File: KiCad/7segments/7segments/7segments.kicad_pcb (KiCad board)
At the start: 2 copper layers, 63.5 x 59.7 mm, 19 parts, among them J1 Conn_01x04_Female, J2 12V DC, J3 R pinnen RGB strips, SW1 ENABLE, SW2 BOOT, T1 BC848, T2 BC848, T3 BC848, T4 BC848, T5 BC848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

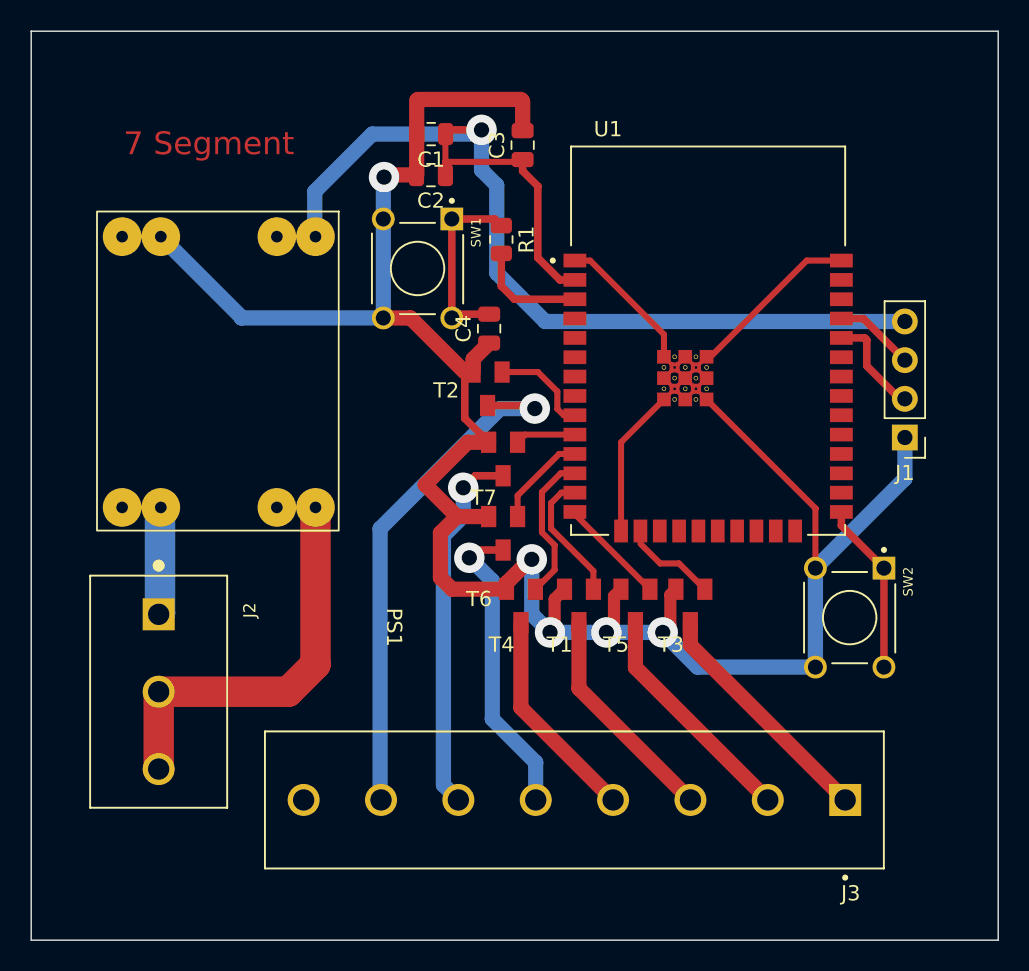
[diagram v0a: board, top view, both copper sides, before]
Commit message: update buffer
enkel schema van de buffer is volledig in orde met LDO!!!
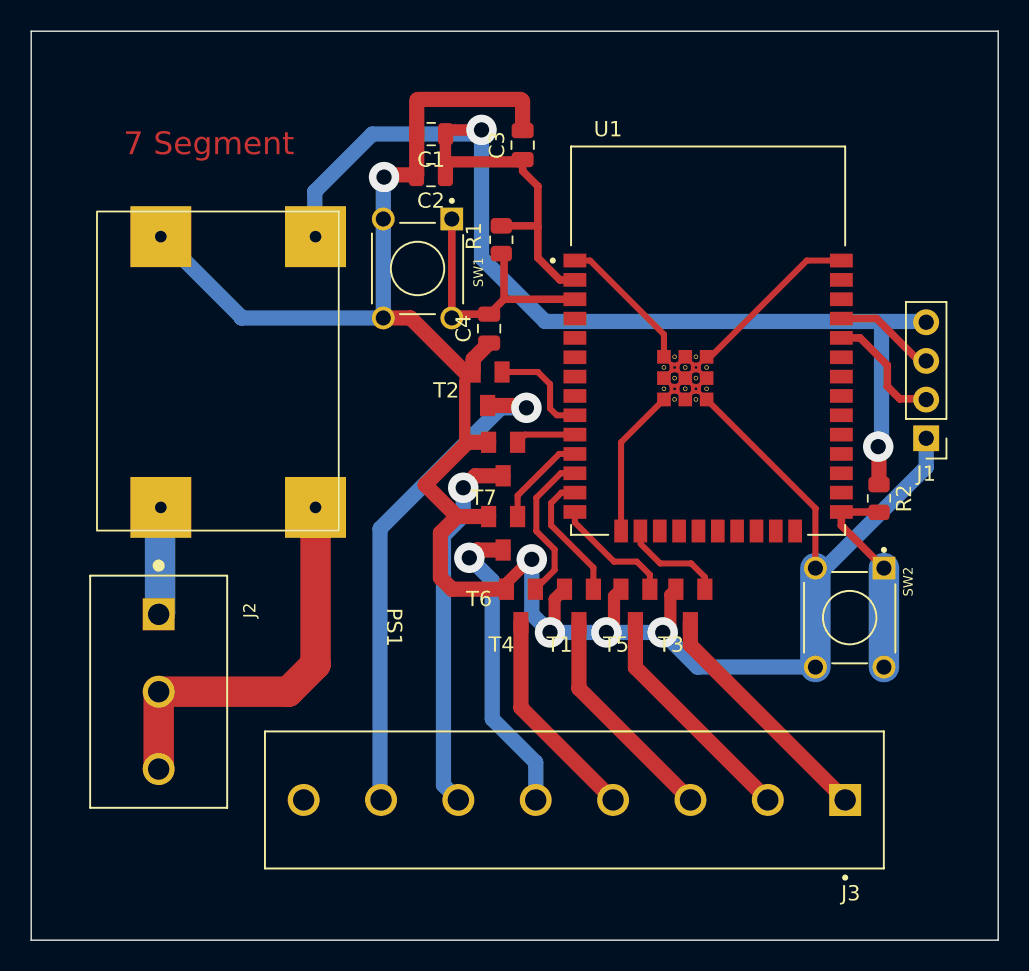
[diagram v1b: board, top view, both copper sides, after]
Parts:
- added R2: 10k, Resistor_SMD:R_0805_2012Metric, F.Cu at (168.7, 101.8)
- moved J1 1.40 mm to (171.8, 97.8)
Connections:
- C4 pad 2: Net-(C4-Pad2) -> Net-(U1-Pad3)
- R1 pad 1: Net-(C4-Pad2) -> +3V3
- R1 pad 2: Net-(R1-Pad2) -> Net-(U1-Pad3)
- SW1 pad 1: Net-(C4-Pad2) -> Net-(U1-Pad3)
- SW1 pad 2: Net-(C4-Pad2) -> Net-(U1-Pad3)
- U1 pad 3: Net-(R1-Pad2) -> Net-(U1-Pad3)
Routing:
- net Net-(U1-Pad3): track 0.00 -> 18.2 mm
- net +3V3: track 74.6 -> 88.8 mm, vias 1 -> 2
- net Net-(C4-Pad2): track 12.5 -> 0.00 mm
- net Net-(R1-Pad2): track 7.33 -> 0.00 mm
- net Net-(U1-Pad25): track 11.3 -> 13.8 mm
- net Net-(J3-Pad7): track 34.4 -> 33.3 mm
- net Net-(J1-Pad3): track 5.57 -> 6.52 mm
- net Net-(T5-Pad1): track 7.11 -> 7.99 mm
- net Net-(J1-Pad2): track 6.94 -> 7.71 mm
